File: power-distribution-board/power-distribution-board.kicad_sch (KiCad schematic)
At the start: 19 parts, among them J1 Conn_01x02, J2 Conn_01x02, J3 Conn_01x02, J4 Conn_01x02, J5 Conn_01x02, J6 Conn_01x02, J7 Conn_01x02, J8 Conn_01x02

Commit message: 完成
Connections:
- net GND: now also D1.1 (K); no longer R1.2
- net VCC: now also R1.1; no longer D1.2 (A)
- new net: D1.2 (A), R1.2
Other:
- moved on the sheet: D1, R1
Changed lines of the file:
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@@
 	(symbol
 		(lib_id "Device:R")
-		(at 46.99 134.62 90)
+		(at 36.83 134.62 90)
 		(unit 1)
 		(exclude_from_sim no)
@@
 		(dnp no)
 		(property "Reference" "R1"
-			(at 46.99 130.302 90)
+			(at 36.83 130.302 90)
 			(effects
 				(font
@@
 		)
 		(property "Value" "1k"
-			(at 46.99 131.826 90)
+			(at 36.83 131.826 90)
 			(effects
 				(font
@@
 		)
 		(property "Footprint" "Resistor_SMD:R_0603_1608Metric_Pad0.98x0.95mm_HandSolder"
-			(at 46.99 136.398 90)
+			(at 36.83 136.398 90)
 			(effects
 				(font
@@
 		)
 		(property "Datasheet" "~"
-			(at 46.99 134.62 0)
+			(at 36.83 134.62 0)
 			(effects
 				(font
@@
 		)
 		(property "Description" ""
-			(at 46.99 134.62 0)
+			(at 36.83 134.62 0)
 			(effects
 				(font
@@
 		)
 		(property "Sim.Device" ""
-			(at 46.99 134.62 0)
+			(at 36.83 134.62 0)
 			(effects
 				(font
@@
 		)
 		(property "Sim.Pins" ""
-			(at 46.99 134.62 0)
+			(at 36.83 134.62 0)
 			(effects
 				(font
@@
 	(symbol
 		(lib_id "Device:LED")
-		(at 36.83 134.62 180)
+		(at 46.99 134.62 180)
 		(unit 1)
 		(exclude_from_sim no)
@@
 		(dnp no)
 		(property "Reference" "D1"
-			(at 36.83 130.302 0)
+			(at 46.99 130.302 0)
 			(effects
 				(font
@@
 		)
 		(property "Value" "LED"
-			(at 36.83 132.08 0)
+			(at 46.99 132.08 0)
 			(effects
 				(font
@@
 		)
 		(property "Footprint" "LED_SMD:LED_0603_1608Metric_Pad1.05x0.95mm_HandSolder"
-			(at 36.83 134.62 0)
+			(at 46.99 134.62 0)
 			(effects
 				(font
@@
 		)
 		(property "Datasheet" "~"
-			(at 36.83 134.62 0)
+			(at 46.99 134.62 0)
 			(effects
 				(font
@@
 		)
 		(property "Description" ""
-			(at 36.83 134.62 0)
+			(at 46.99 134.62 0)
 			(effects
 				(font
@@
 		)
 		(property "Sim.Device" ""
-			(at 36.83 134.62 0)
+			(at 46.99 134.62 0)
 			(effects
 				(font
@@
 		)
 		(property "Sim.Pins" ""
-			(at 36.83 134.62 0)
-			(effects
-				(font
+			(at 46.99 134.62 0)
+			(effects
+				(font

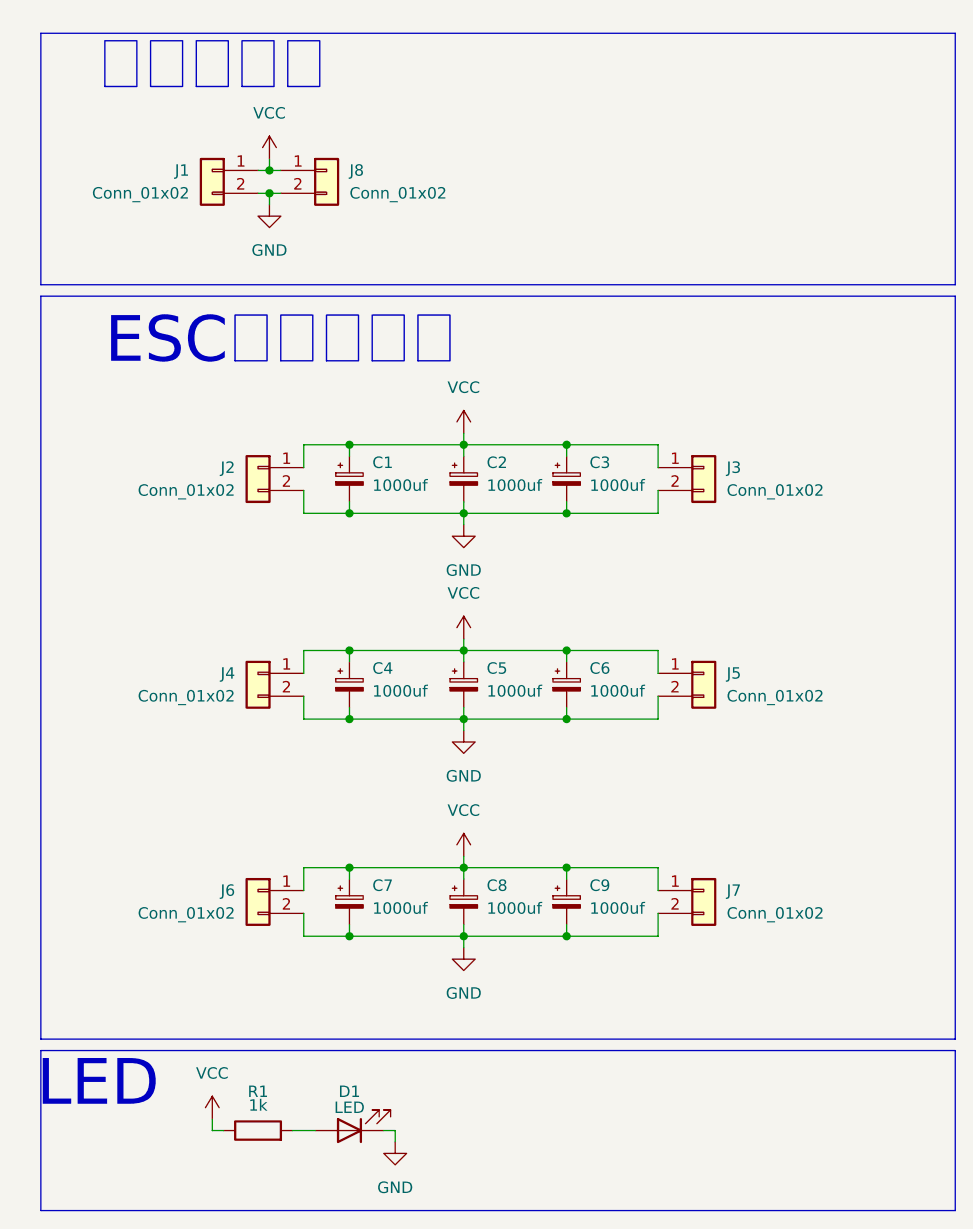
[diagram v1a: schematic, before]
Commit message: ±の反転を修正 ガーバ生成
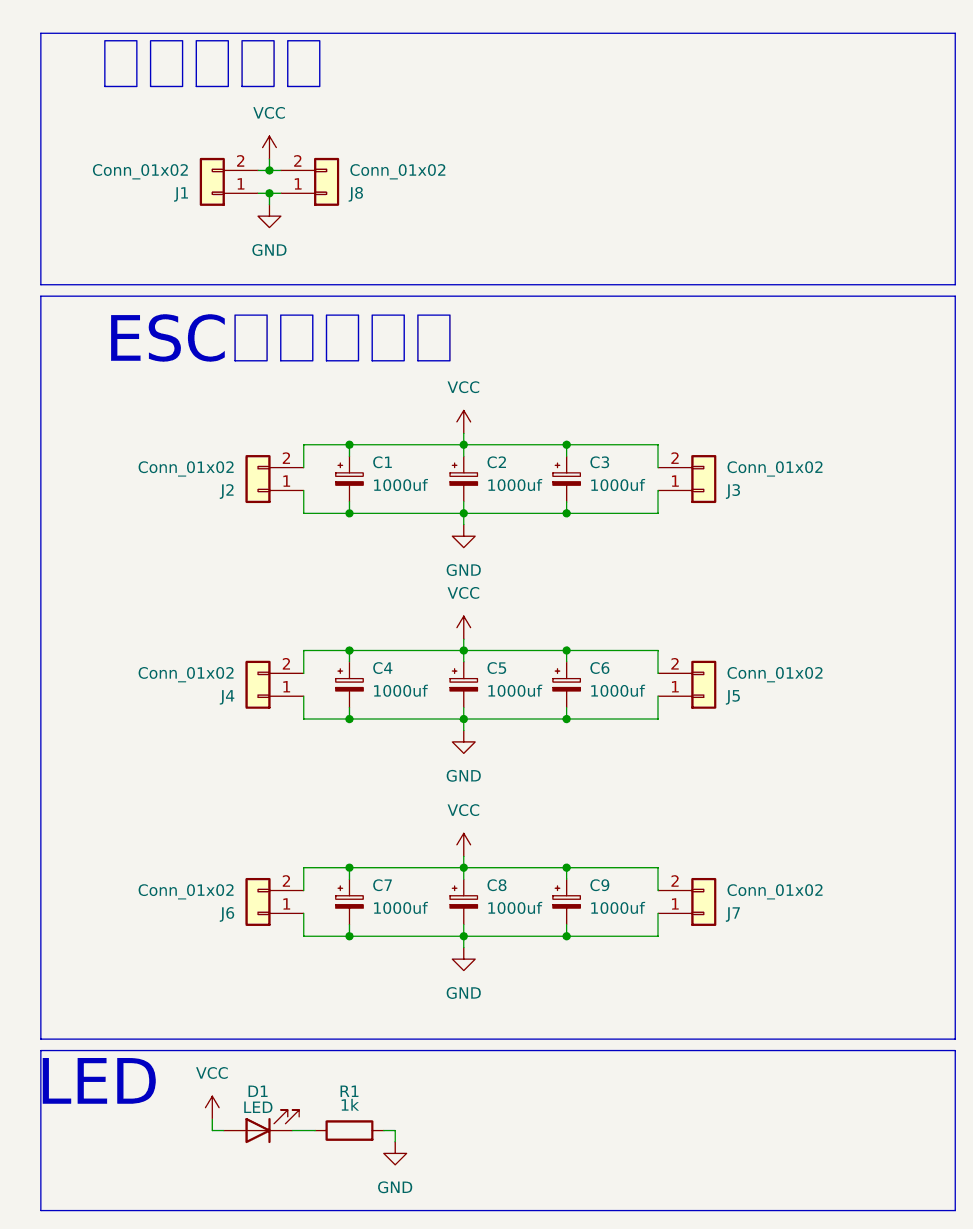
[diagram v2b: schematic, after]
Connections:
- net GND: now also J1.1 (Pin_1), J2.1 (Pin_1), J3.1 (Pin_1), J4.1 (Pin_1), J5.1 (Pin_1), J6.1 (Pin_1), J7.1 (Pin_1), J8.1 (Pin_1), R1.2; no longer D1.1 (K), J1.2 (Pin_2), J2.2 (Pin_2), J3.2 (Pin_2), J4.2 (Pin_2), J5.2 (Pin_2), J6.2 (Pin_2), J7.2 (Pin_2), J8.2 (Pin_2)
- net VCC: now also D1.2 (A), J1.2 (Pin_2), J2.2 (Pin_2), J3.2 (Pin_2), J4.2 (Pin_2), J5.2 (Pin_2), J6.2 (Pin_2), J7.2 (Pin_2), J8.2 (Pin_2); no longer J1.1 (Pin_1), J2.1 (Pin_1), J3.1 (Pin_1), J4.1 (Pin_1), J5.1 (Pin_1), J6.1 (Pin_1), J7.1 (Pin_1), J8.1 (Pin_1), R1.1
- new net: D1.1 (K), R1.1
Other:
- moved on the sheet: D1, J1, J2, J4, J6, R1
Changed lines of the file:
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@@
 	(symbol
 		(lib_id "Device:R")
-		(at 36.83 134.62 90)
+		(at 46.99 134.62 90)
 		(unit 1)
 		(exclude_from_sim no)
@@
 		(dnp no)
 		(property "Reference" "R1"
-			(at 36.83 130.302 90)
+			(at 46.99 130.302 90)
 			(effects
 				(font
@@
 		)
 		(property "Value" "1k"
-			(at 36.83 131.826 90)
+			(at 46.99 131.826 90)
 			(effects
 				(font
@@
 		)
 		(property "Footprint" "Resistor_SMD:R_0603_1608Metric_Pad0.98x0.95mm_HandSolder"
-			(at 36.83 136.398 90)
+			(at 46.99 136.398 90)
 			(effects
 				(font
@@
 		)
 		(property "Datasheet" "~"
-			(at 36.83 134.62 0)
+			(at 46.99 134.62 0)
 			(effects
 				(font
@@
 		)
 		(property "Description" ""
-			(at 36.83 134.62 0)
+			(at 46.99 134.62 0)
 			(effects
 				(font
@@
 		)
 		(property "Sim.Device" ""
-			(at 36.83 134.62 0)
+			(at 46.99 134.62 0)
 			(effects
 				(font
@@
 		)
 		(property "Sim.Pins" ""
-			(at 36.83 134.62 0)
+			(at 46.99 134.62 0)
 			(effects
 				(font
@@
 	(symbol
 		(lib_id "Connector_Generic:Conn_01x02")
-		(at 36.83 107.95 0)
-		(mirror y)
+		(at 36.83 110.49 180)
 		(unit 1)
 		(exclude_from_sim no)
@@
 		(dnp no)
 		(property "Reference" "J6"
-			(at 34.29 107.9499 0)
+			(at 34.29 110.4901 0)
 			(effects
 				(font
@@
 		)
 		(property "Value" "Conn_01x02"
-			(at 34.29 110.4899 0)
+			(at 34.29 107.9501 0)
 			(effects
 				(font
@@
 		)
 		(property "Footprint" "0Ikedalibrary:AMASS_XT60-F_1x02_P7.20mm_Vertical"
-			(at 36.83 107.95 0)
+			(at 36.83 110.49 0)
 			(effects
 				(font
@@
 		)
 		(property "Datasheet" "~"
-			(at 36.83 107.95 0)
+			(at 36.83 110.49 0)
 			(effects
 				(font
@@
 		)
 		(property "Description" "Generic connector, single row, 01x02, script generated (kicad-library-utils/schlib/autogen/connector/)"
-			(at 36.83 107.95 0)
+			(at 36.83 110.49 0)
 			(effects
 				(font
@@
 	(symbol
 		(lib_id "Connector_Generic:Conn_01x02")
-		(at 44.45 27.94 0)
+		(at 44.45 30.48 0)
+		(mirror x)
 		(unit 1)
 		(exclude_from_sim no)
@@
 		(dnp no)
 		(property "Reference" "J8"
-			(at 46.99 27.9399 0)
+			(at 46.99 30.4801 0)
 			(effects
 				(font
@@
 		)
 		(property "Value" "Conn_01x02"
-			(at 46.99 30.4799 0)
+			(at 46.99 27.9401 0)
 			(effects
 				(font
@@
 		)
 		(property "Footprint" "0Ikedalibrary:AMASS_XT60-M_1x02_P7.20mm_Vertical"
-			(at 44.45 27.94 0)
+			(at 44.45 30.48 0)
 			(effects
 				(font
@@
 		)
 		(property "Datasheet" "~"
-			(at 44.45 27.94 0)
+			(at 44.45 30.48 0)
 			(effects
 				(font
@@
 		)
 		(property "Description" "Generic connector, single row, 01x02, script generated (kicad-library-utils/schlib/autogen/connector/)"
-			(at 44.45 27.94 0)
+			(at 44.45 30.48 0)
 			(effects
 				(font
@@
 	(symbol
 		(lib_id "Connector_Generic:Conn_01x02")
-		(at 36.83 83.82 0)
-		(mirror y)
+		(at 36.83 86.36 180)
 		(unit 1)
 		(exclude_from_sim no)
@@
 		(dnp no)
 		(property "Reference" "J4"
-			(at 34.29 83.8199 0)
+			(at 34.29 86.3601 0)
 			(effects
 				(font
@@
 		)
 		(property "Value" "Conn_01x02"
-			(at 34.29 86.3599 0)
+			(at 34.29 83.8201 0)
 			(effects
 				(font
@@
 		)
 		(property "Footprint" "0Ikedalibrary:AMASS_XT60-F_1x02_P7.20mm_Vertical"
-			(at 36.83 83.82 0)
+			(at 36.83 86.36 0)
 			(effects
 				(font
@@
 		)
 		(property "Datasheet" "~"
-			(at 36.83 83.82 0)
+			(at 36.83 86.36 0)
 			(effects
 				(font
@@
 		)
 		(property "Description" "Generic connector, single row, 01x02, script generated (kicad-library-utils/schlib/autogen/connector/)"
-			(at 36.83 83.82 0)
+			(at 36.83 86.36 0)
 			(effects
 				(font
@@
 	(symbol
 		(lib_id "Connector_Generic:Conn_01x02")
-		(at 36.83 60.96 0)
-		(mirror y)
+		(at 36.83 63.5 180)
 		(unit 1)
 		(exclude_from_sim no)
@@
 		(dnp no)
 		(property "Reference" "J2"
-			(at 34.29 60.9599 0)
+			(at 34.29 63.5001 0)
 			(effects
 				(font
@@
 		)
 		(property "Value" "Conn_01x02"
-			(at 34.29 63.4999 0)
+			(at 34.29 60.9601 0)
 			(effects
 				(font
@@
 		)
 		(property "Footprint" "0Ikedalibrary:AMASS_XT60-F_1x02_P7.20mm_Vertical"
-			(at 36.83 60.96 0)
+			(at 36.83 63.5 0)
 			(effects
 				(font
@@
 		)
 		(property "Datasheet" "~"
-			(at 36.83 60.96 0)
+			(at 36.83 63.5 0)
 			(effects
 				(font
@@
 		)
 		(property "Description" "Generic connector, single row, 01x02, script generated (kicad-library-utils/schlib/autogen/connector/)"
-			(at 36.83 60.96 0)
+			(at 36.83 63.5 0)
 			(effects
 				(font
@@
 	(symbol
 		(lib_id "Connector_Generic:Conn_01x02")
-		(at 86.36 60.96 0)
+		(at 86.36 63.5 0)
+		(mirror x)
 		(unit 1)
 		(exclude_from_sim no)
@@
 		(dnp no)
 		(property "Reference" "J3"
-			(at 88.9 60.9599 0)
+			(at 88.9 63.5001 0)
 			(effects
 				(font
@@
 		)
 		(property "Value" "Conn_01x02"
-			(at 88.9 63.4999 0)
+			(at 88.9 60.9601 0)
 			(effects
 				(font
@@
 		)
 		(property "Footprint" "0Ikedalibrary:AMASS_XT60-F_1x02_P7.20mm_Vertical"
-			(at 86.36 60.96 0)
+			(at 86.36 63.5 0)
 			(effects
 				(font
@@
 		)
 		(property "Datasheet" "~"
-			(at 86.36 60.96 0)
+			(at 86.36 63.5 0)
 			(effects
 				(font
@@
 		)
 		(property "Description" "Generic connector, single row, 01x02, script generated (kicad-library-utils/schlib/autogen/connector/)"
-			(at 86.36 60.96 0)
+			(at 86.36 63.5 0)
 			(effects
 				(font
@@
 	(symbol
 		(lib_id "Connector_Generic:Conn_01x02")
-		(at 86.36 107.95 0)
+		(at 86.36 110.49 0)
+		(mirror x)
 		(unit 1)
 		(exclude_from_sim no)
@@
 		(dnp no)
 		(property "Reference" "J7"
-			(at 88.9 107.9499 0)
+			(at 88.9 110.4901 0)
 			(effects
 				(font
@@
 		)
 		(property "Value" "Conn_01x02"
-			(at 88.9 110.4899 0)
+			(at 88.9 107.9501 0)
 			(effects
 				(font
@@
 		)
 		(property "Footprint" "0Ikedalibrary:AMASS_XT60-F_1x02_P7.20mm_Vertical"
-			(at 86.36 107.95 0)
+			(at 86.36 110.49 0)
 			(effects
 				(font
@@
 		)
 		(property "Datasheet" "~"
-			(at 86.36 107.95 0)
+			(at 86.36 110.49 0)
 			(effects
 				(font
@@
 		)
 		(property "Description" "Generic connector, single row, 01x02, script generated (kicad-library-utils/schlib/autogen/connector/)"
-			(at 86.36 107.95 0)
+			(at 86.36 110.49 0)
 			(effects
 				(font
@@
 	(symbol
 		(lib_id "Connector_Generic:Conn_01x02")
-		(at 86.36 83.82 0)
+		(at 86.36 86.36 0)
+		(mirror x)
 		(unit 1)
 		(exclude_from_sim no)
@@
 		(dnp no)
 		(property "Reference" "J5"
-			(at 88.9 83.8199 0)
+			(at 88.9 86.3601 0)
 			(effects
 				(font
@@
 		)
 		(property "Value" "Conn_01x02"
-			(at 88.9 86.3599 0)
+			(at 88.9 83.8201 0)
 			(effects
 				(font
@@
 		)
 		(property "Footprint" "0Ikedalibrary:AMASS_XT60-F_1x02_P7.20mm_Vertical"
-			(at 86.36 83.82 0)
+			(at 86.36 86.36 0)
 			(effects
 				(font
@@
 		)
 		(property "Datasheet" "~"
-			(at 86.36 83.82 0)
+			(at 86.36 86.36 0)
 			(effects
 				(font
@@
 		)
 		(property "Description" "Generic connector, single row, 01x02, script generated (kicad-library-utils/schlib/autogen/connector/)"
-			(at 86.36 83.82 0)
+			(at 86.36 86.36 0)
 			(effects
 				(font
@@
 	(symbol
 		(lib_id "Device:LED")
-		(at 46.99 134.62 180)
+		(at 36.83 134.62 180)
 		(unit 1)
 		(exclude_from_sim no)
@@
 		(dnp no)
 		(property "Reference" "D1"
-			(at 46.99 130.302 0)
+			(at 36.83 130.302 0)
 			(effects
 				(font
@@
 		)
 		(property "Value" "LED"
-			(at 46.99 132.08 0)
+			(at 36.83 132.08 0)
 			(effects
 				(font
@@
 		)
 		(property "Footprint" "LED_SMD:LED_0603_1608Metric_Pad1.05x0.95mm_HandSolder"
-			(at 46.99 134.62 0)
+			(at 36.83 134.62 0)
 			(effects
 				(font
@@
 		)
 		(property "Datasheet" "~"
-			(at 46.99 134.62 0)
+			(at 36.83 134.62 0)
 			(effects
 				(font
@@
 		)
 		(property "Description" ""
-			(at 46.99 134.62 0)
+			(at 36.83 134.62 0)
 			(effects
 				(font
@@
 		)
 		(property "Sim.Device" ""
-			(at 46.99 134.62 0)
+			(at 36.83 134.62 0)
 			(effects
 				(font
@@
 		)
 		(property "Sim.Pins" ""
-			(at 46.99 134.62 0)
+			(at 36.83 134.62 0)
 			(effects
 				(font
@@
 	(symbol
 		(lib_id "Connector_Generic:Conn_01x02")
-		(at 31.75 27.94 0)
-		(mirror y)
+		(at 31.75 30.48 180)
 		(unit 1)
 		(exclude_from_sim no)
@@
 		(dnp no)
 		(property "Reference" "J1"
-			(at 29.21 27.9399 0)
+			(at 29.21 30.4801 0)
 			(effects
 				(font
@@
 		)
 		(property "Value" "Conn_01x02"
-			(at 29.21 30.4799 0)
+			(at 29.21 27.9401 0)
 			(effects
 				(font
@@
 		)
 		(property "Footprint" "0Ikedalibrary:AMASS_XT60-F_1x02_P7.20mm_Vertical"
-			(at 31.75 27.94 0)
+			(at 31.75 30.48 0)
 			(effects
 				(font
@@
 		)
 		(property "Datasheet" "~"
-			(at 31.75 27.94 0)
+			(at 31.75 30.48 0)
 			(effects
 				(font
@@
 		)
 		(property "Description" "Generic connector, single row, 01x02, script generated (kicad-library-utils/schlib/autogen/connector/)"
-			(at 31.75 27.94 0)
-			(effects
-				(font
+			(at 31.75 30.48 0)
+			(effects
+				(font
